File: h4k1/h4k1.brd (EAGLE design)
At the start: 1438.9 x 393.4 mm, 159 parts, among them IC1 STM32F10XCXT6, K1 CHERRY-MX-LED, K10 CHERRY-MX-LED, K11 CHERRY-MX-LED, K12 CHERRY-MX-LED, K13 CHERRY-MX-LED, K14 CHERRY-MX-LED, K15 CHERRY-MX-LED, K16 CHERRY-MX-LED, K17 CHERRY-MX-LED, K18 CHERRY-MX-LED, K19 CHERRY-MX-LED, K2 CHERRY-MX-LED, K20 CHERRY-MX-LED, K21 CHERRY-MX-LED, K22 CHERRY-MX-LED, K23 CHERRY-MX-LED, K24 CHERRY-MX-LED, K25 CHERRY-MX-LED, K26 CHERRY-MX-LED, K27 CHERRY-MX-LED, K28 CHERRY-MX-LED, K29 CHERRY-MX-LED, K3 CHERRY-MX-LED, K30 CHERRY-MX-LED, K31 CHERRY-MX-LED, K32 CHERRY-MX-LED, K33 CHERRY-MX-LED, K34 CHERRY-MX-LED, K35 CHERRY-MX-LED, K36 CHERRY-MX-LED, K37 CHERRY-MX-LED, K38 CHERRY-MX-LED, K39 CHERRY-MX-LED, K4 CHERRY-MX-LED, K40 CHERRY-MX-LED, K41 CHERRY-MX-LED, K42 CHERRY-MX-LED, K43 CHERRY-MX-LED, K44 CHERRY-MX-LED, K45 CHERRY-MX-LED, K46 CHERRY-MX-LED, K47 CHERRY-MX-LED, K48 CHERRY-MX-LED, K49 CHERRY-MX-LED, K5 CHERRY-MX-LED, K50 CHERRY-MX-LED, K51 CHERRY-MX-LED, K52 CHERRY-MX-LED, K53 CHERRY-MX-LED, K54 CHERRY-MX-LED, K55 CHERRY-MX-LED, K56 CHERRY-MX-LED, K57 CHERRY-MX-LED, K58 CHERRY-MX-LED, K59 CHERRY-MX-LED, K6 CHERRY-MX-LED, K60 CHERRY-MX-LED, K61 CHERRY-MX-LED, K62 CHERRY-MX-LED, K63 CHERRY-MX-LED, K64 CHERRY-MX-LED, K7 CHERRY-MX-LED, K8 CHERRY-MX-LED, K9 CHERRY-MX-LED

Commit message: add usb hub
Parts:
- added C10, C11: 4.7uF, hqc-basic:0603
- added C12, C13, C14, C15, C16, C18: 100nF, hqc-basic:0603
- added C17, C19: 10uF, hqc-basic:0603
- added L2: 10uH, hqc-basic:0603
- added R19: 0, hqc-basic:0603
- added R20: 680, hqc-basic:0603
- added R21, R22, R23, R24, R25: 10k, hqc-basic:0603
- added U1: G850G, hqc-communication:SSOP28
- added U2: (no value), hqc-power:SOT223
- added X3: (no value), hqc-crystal:49S
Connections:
- new net 3V3: C18.P$2, C19.P$2, L2.P$1, R22.P$2, U1.16, U1.24, U2.2
- new net 5V: C16.P$2, C17.P$2, R19.P$2, R21.P$1, R25.P$2, U1.23, U2.3
- new net AVDD: C12.P$2, C13.P$2, C14.P$2, L2.P$2, U1.1, U1.10, U1.5
- new net HOST_USB+: U1.26
- new net HOST_USB-: U1.25
- new net N$24: C15.P$2, R21.P$2, U1.13
- new net N$26: R20.P$2, U1.4
- new net N$28: R22.P$1, U1.18
- new net N$30: R23.P$1, U1.17
- new net N$34: R24.P$1, R25.P$1, U1.21
- new net USB1+: U1.28
- new net USB1-: U1.27
- new net USB2+: U1.3
- new net USB2-: U1.2
- new net USB3+: U1.9
- new net USB3-: U1.8
- new net USB4+: U1.12
- new net USB4-: U1.11
- new net VBUS: R19.P$1
- new net X1: C10.P$2, U1.6, X3.P$1
- new net X2: C11.P$2, U1.7, X3.P$2
- net GND: now also C10.P$1, C11.P$1, C12.P$1, C13.P$1, C14.P$1, C15.P$1, C16.P$1, C17.P$1, C18.P$1, C19.P$1, R20.P$1, R23.P$2, R24.P$2, U1.14, U1.15, U2.1

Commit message: audio done
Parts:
- added C20, C21: (no value), hqc:0805
- added C22, C23, C24, C25, C26: 1uF, hqc:0805
- added C27: 10uF, hqc:3216-CPOL
- added C28, C29: 22nF, hqc:0805
- added C30, C31: 100uF, hqc:7343-CPOL
- added C32, C33: 1uF, hqc:3216-CPOL
- added J1: (no value), hqc-connector:PH-5AWD
- added J2: PJ-313D-AUDIO-JACK, hqc:PJ-313D
- added R26: 1M, hqc:0805
- added R27, R28: 1.5k, hqc:0805
- added R29, R30: 22, hqc:0805
- added R31, R32: 16, hqc:0805
- added R33, R34: 330, hqc:0805
- added U3: PCM2704CDB, hqc:SSOP28
- added X4: 12M, hqc-crystal:49S
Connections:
- new net AUDIO_L: C32.P$1, J2.P3, J2.P3@2
- new net AUDIO_R: C33.P$1, J2.P2, J2.P2@2
- new net N$32: C20.P$2, R26.P$1, U3.1, X4.P$1
- new net N$36: C21.P$1, R26.P$2, U3.28, X4.P$2
- new net N$38: R29.P$2, U3.8
- new net N$40: R30.P$2, U3.9
- new net N$42: C22.P$1, R27.P$1, R28.P$2, U3.21, U3.25, U3.26, U3.4, U3.7
- new net N$44: C25.P$1, U3.20
- new net N$46: C30.P$2, C32.P$2, R33.P$2
- new net N$48: C24.P$1, U3.13
- new net N$50: R27.P$2, U3.3
- new net N$54: C26.P$1, U3.16
- new net N$55: C27.P$1, U3.18
- new net N$62: C31.P$2, C33.P$2, R34.P$2
- new net N$64: C29.P$1, R32.P$2
- new net N$66: C28.P$1, R31.P$2
- new net SHIELD: J1.P$5
- new net VOUT_L: C28.P$2, C30.P$1, U3.14
- new net VOUT_R: C29.P$2, C31.P$1, U3.15
- net GND: now also C20.P$1, C21.P$2, C22.P$2, C23.P$1, C24.P$2, C25.P$2, C26.P$2, C27.P$2, J1.P$4, J2.P1, J2.P1@2, R31.P$1, R32.P$1, R33.P$1, R34.P$1, U3.11, U3.12, U3.17, U3.19, U3.6
- net HOST_USB+: now also J1.P$3
- net HOST_USB-: now also J1.P$2
- net USB1+: now also R28.P$1, R30.P$1
- net USB1-: now also R29.P$1
- net VBUS: now also C23.P$2, J1.P$1, U3.10
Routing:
- net GND: track 0.00 -> 115.7 mm, vias 0 -> 6
- net N$42: track 0.00 -> 36.3 mm
- net VBUS: track 0.00 -> 27.1 mm, vias 0 -> 2
- net N$36: track 0.00 -> 17.3 mm
- net N$62: track 0.00 -> 16.2 mm
- net N$32: track 0.00 -> 16.1 mm
- net N$46: track 0.00 -> 14.8 mm
- net VOUT_L: track 0.00 -> 12.6 mm
- net VOUT_R: track 0.00 -> 12.5 mm
- net N$40: track 0.00 -> 7.47 mm
- net N$48: track 0.00 -> 7.18 mm
- net N$38: track 0.00 -> 6.95 mm
- net N$50: track 0.00 -> 4.98 mm
- net N$54: track 0.00 -> 4.80 mm
- net USB1+: track 0.00 -> 4.60 mm
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- added copper zone on layer 1, net GND
- added copper zone on layer 16, net GND

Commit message: add usb connector
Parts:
- added J3: USB-AF10, hqc:USB-AF10
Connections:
- net GND: now also J3.P$G
- net USB1+: now also J3.P$D+; no longer R28.P$1, R30.P$1
- net USB1-: now also J3.P$D-; no longer R29.P$1
- net USB2+: now also R28.P$1, R30.P$1
- net USB2-: now also R29.P$1
- net VBUS: now also J3.P$V
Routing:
- net USB1+: track 4.60 -> 0.00 mm
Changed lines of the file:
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@@
 <element name="C33" library="hqc" package="3216-CPOL" value="1uF" x="197.8025" y="285.75" rot="R180"/>
 <element name="J2" library="hqc" package="PJ-313D" value="PJ-313D-AUDIO-JACK" x="223.8375" y="281.6225" rot="R180"/>
+<element name="J3" library="hqc" package="USB-AF10" value="USB-AF10" x="-145.415" y="-289.2425"/>
 </elements>
 <signals>
@@
 <contactref element="J2" pad="P1"/>
 <contactref element="J2" pad="P1@2"/>
+<contactref element="J3" pad="P$G"/>
 <wire x1="-144.2593" y1="-105.41" x2="-144.2593" y2="-110.49" width="0" layer="19" extent="1-1"/>
 <wire x1="-144.2593" y1="-100.33" x2="-144.2593" y2="-105.41" width="0" layer="19" extent="1-1"/>
@@
 <wire x1="-151.6507" y1="-254" x2="-151.6507" y2="-248.92" width="0" layer="19" extent="1-1"/>
 <wire x1="-149.86" y1="-272.51" x2="-151.6507" y2="-254" width="0" layer="19" extent="1-1"/>
+<wire x1="-141.915" y1="-277.8725" x2="-149.86" y2="-272.51" width="0" layer="19" extent="1-1"/>
 <wire x1="172.4025" y1="265.7475" x2="-135.2" y2="-76.49" width="0" layer="19" extent="1-1"/>
 <wire x1="176.825" y1="275.775" x2="180.0225" y2="275.7225" width="0" layer="19" extent="1-1"/>
-<wire x1="223.8375" y1="278.4225" x2="191.135" y2="286.0675" width="0" layer="19" extent="1-16"/>
+<wire x1="223.8375" y1="278.4225" x2="191.135" y2="279.0825" width="0" layer="19" extent="1-1"/>
 <wire x1="223.8375" y1="284.8225" x2="223.8375" y2="278.4225" width="0" layer="19" extent="1-1"/>
 </signal>
@@
 <wire x1="187.325" y1="272.7325" x2="187.325" y2="265.43" width="0.3048" layer="16"/>
 <wire x1="187.325" y1="270.8275" x2="187.325" y2="272.7325" width="0.3048" layer="1"/>
+<contactref element="J3" pad="P$V"/>
 <wire x1="-153.1493" y1="-173.99" x2="187.325" y2="265.43" width="0" layer="19" extent="1-16"/>
 <wire x1="-149.86" y1="-266.51" x2="-153.1493" y2="-173.99" width="0" layer="19" extent="1-1"/>
+<wire x1="-148.915" y1="-277.8725" x2="-149.86" y2="-266.51" width="0" layer="19" extent="1-1"/>
 </signal>
 <signal name="5V">
@@
 <signal name="USB2-">
 <contactref element="U1" pad="2"/>
+<contactref element="R29" pad="P$1"/>
+<wire x1="-149.625" y1="-153.485" x2="181.61" y2="268.9225" width="0" layer="19" extent="1-1"/>
 </signal>
 <signal name="USB2+">
 <contactref element="U1" pad="3"/>
+<contactref element="R30" pad="P$1"/>
+<contactref element="R28" pad="P$1"/>
+<wire x1="179.705" y1="268.9225" x2="183.515" y2="268.9225" width="0" layer="19" extent="1-1"/>
+<wire x1="-148.975" y1="-153.485" x2="179.705" y2="268.9225" width="0" layer="19" extent="1-1"/>
 </signal>
 <signal name="AVDD">
@@
 <signal name="USB1+">
 <contactref element="U1" pad="28"/>
-<contactref element="R30" pad="P$1"/>
-<contactref element="R28" pad="P$1"/>
-<wire x1="179.705" y1="268.9225" x2="180.6575" y2="269.875" width="0.3048" layer="1"/>
-<wire x1="180.6575" y1="269.875" x2="182.5625" y2="269.875" width="0.3048" layer="1"/>
-<wire x1="182.5625" y1="269.875" x2="183.515" y2="268.9225" width="0.3048" layer="1"/>
-<wire x1="-150.275" y1="-146.235" x2="179.705" y2="268.9225" width="0" layer="19" extent="1-1"/>
+<contactref element="J3" pad="P$D+"/>
+<wire x1="-150.275" y1="-146.235" x2="-144.415" y2="-277.8725" width="0" layer="19" extent="1-1"/>
 </signal>
 <signal name="USB1-">
 <contactref element="U1" pad="27"/>
-<contactref element="R29" pad="P$1"/>
-<wire x1="-149.625" y1="-146.235" x2="181.61" y2="268.9225" width="0" layer="19" extent="1-1"/>
+<contactref element="J3" pad="P$D-"/>
+<wire x1="-149.625" y1="-146.235" x2="-146.415" y2="-277.8725" width="0" layer="19" extent="1-1"/>
 </signal>
 <signal name="HOST_USB+">

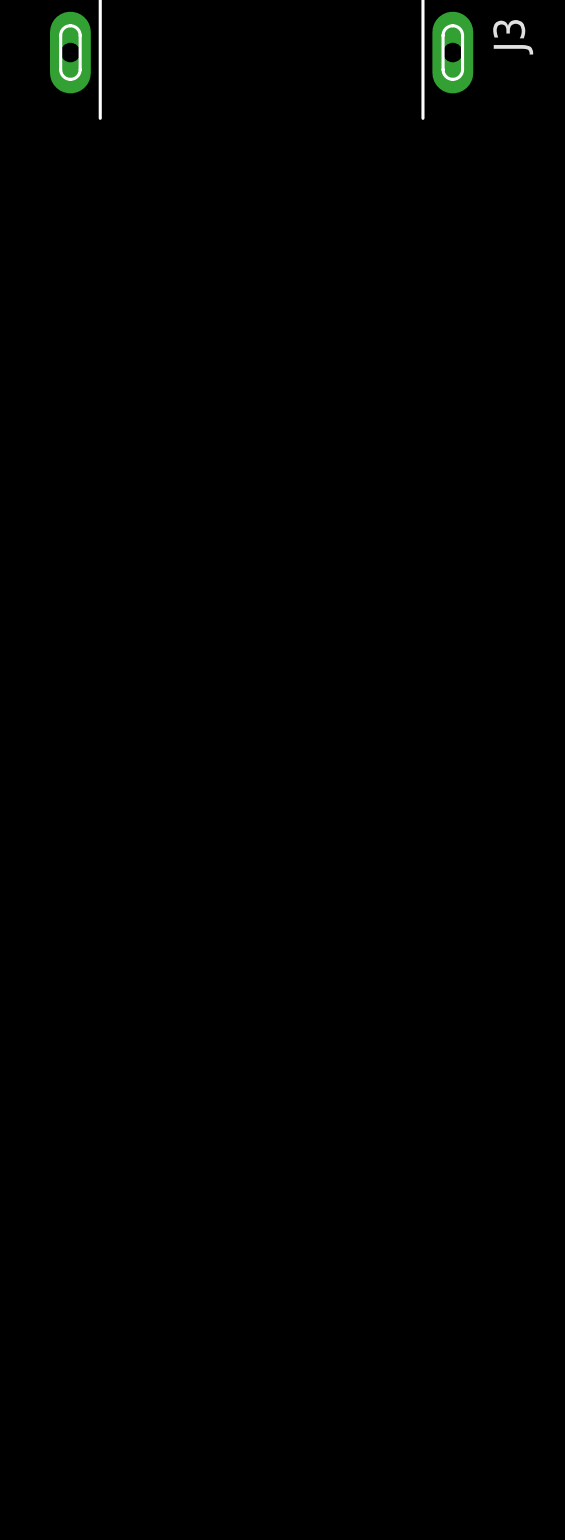
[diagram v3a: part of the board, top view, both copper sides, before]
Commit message: add switches
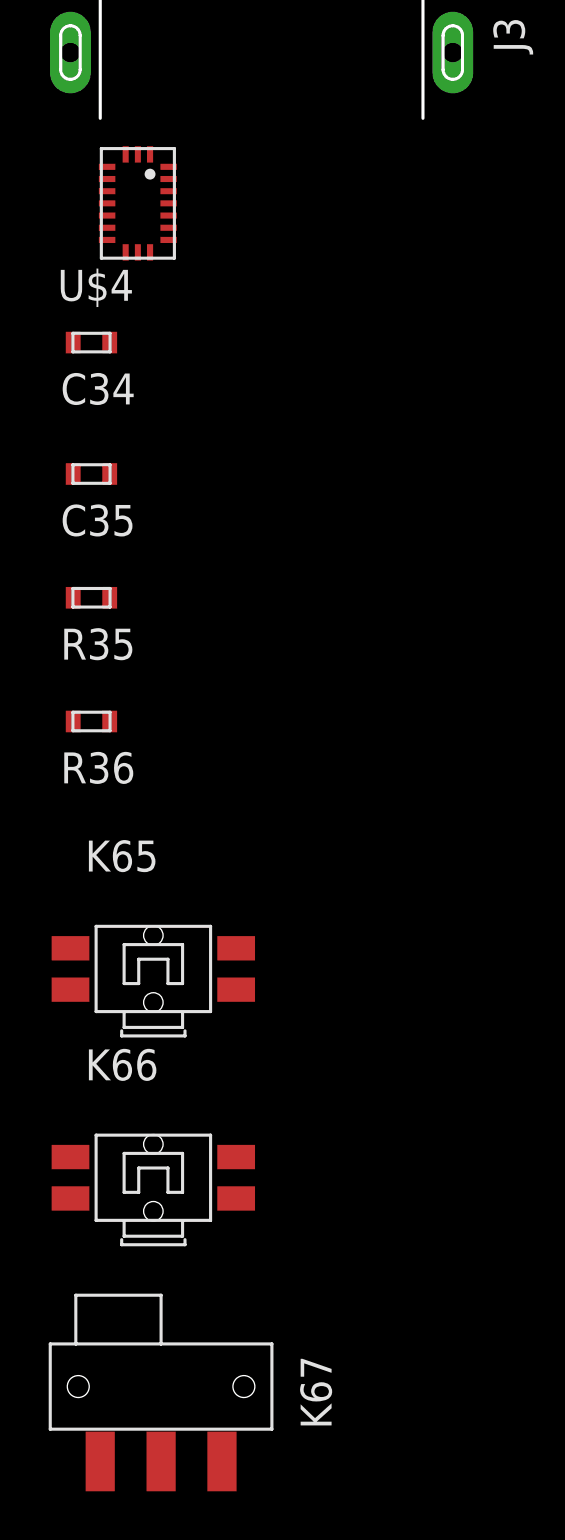
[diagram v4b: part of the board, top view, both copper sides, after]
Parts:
- added C34, C35: 100nF, hqc-basic:0603
- added K65, K66: EVQPUL02K, hqc:EVQPUL
- added K67: K3-1280S-F2, hqc:K3-1280S-F2
- added R35, R36: 4.7k, hqc-basic:0603
- added U$4: BMX055, sensor:BMX055
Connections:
- new net I2C_SCL: IC1.45, R35.P$1, U$4.P$9
- new net I2C_SDA: IC1.46, R36.P$1, U$4.P$11
- net GND: now also C34.P$1, C35.P$1, U$4.P$12, U$4.P$17, U$4.P$20, U$4.P$4, U$4.P$6
- net VDD: now also C34.P$2, C35.P$2, R35.P$2, R36.P$2, U$4.P$13, U$4.P$3, U$4.P$7
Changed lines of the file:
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@@
 <layer number="51" name="tDocu" color="7" fill="1" visible="yes" active="yes"/>
 <layer number="52" name="bDocu" color="7" fill="1" visible="yes" active="yes"/>
+<layer number="53" name="tGND_GNDA" color="7" fill="9" visible="no" active="no"/>
+<layer number="54" name="bGND_GNDA" color="1" fill="9" visible="no" active="no"/>
 <layer number="56" name="wert" color="7" fill="1" visible="no" active="no"/>
 <layer number="90" name="Modules" color="5" fill="1" visible="no" active="no"/>
@@
 <layer number="100" name="Muster" color="7" fill="1" visible="no" active="no"/>
 <layer number="101" name="Patch_Top" color="12" fill="4" visible="yes" active="yes"/>
+<layer number="102" name="Vscore" color="7" fill="1" visible="no" active="yes"/>
+<layer number="104" name="Name" color="7" fill="1" visible="no" active="yes"/>
 <layer number="116" name="Patch_BOT" color="9" fill="4" visible="yes" active="yes"/>
+<layer number="121" name="_tsilk" color="7" fill="1" visible="no" active="yes"/>
+<layer number="122" name="_bsilk" color="7" fill="1" visible="no" active="yes"/>
+<layer number="151" name="HeatSink" color="7" fill="1" visible="no" active="yes"/>
 <layer number="200" name="200bmp" color="1" fill="10" visible="no" active="no"/>
+<layer number="201" name="201bmp" color="2" fill="1" visible="no" active="no"/>
+<layer number="202" name="202bmp" color="3" fill="1" visible="no" active="no"/>
+<layer number="203" name="203bmp" color="4" fill="10" visible="no" active="yes"/>
+<layer number="204" name="204bmp" color="5" fill="10" visible="no" active="yes"/>
+<layer number="205" name="205bmp" color="6" fill="10" visible="no" active="yes"/>
+<layer number="206" name="206bmp" color="7" fill="10" visible="no" active="yes"/>
+<layer number="207" name="207bmp" color="8" fill="10" visible="no" active="yes"/>
+<layer number="208" name="208bmp" color="9" fill="10" visible="no" active="yes"/>
+<layer number="231" name="Eagle3D_PG1" color="14" fill="1" visible="no" active="yes"/>
+<layer number="232" name="Eagle3D_PG2" color="14" fill="2" visible="no" active="yes"/>
+<layer number="233" name="Eagle3D_PG3" color="14" fill="4" visible="no" active="yes"/>
 <layer number="250" name="Descript" color="3" fill="1" visible="no" active="no"/>
 <layer number="251" name="SMDround" color="12" fill="11" visible="no" active="no"/>
@@
 <classes>
 <class number="0" name="default" width="0" drill="0">
+<clearance class="0" value="0.205"/>
 </class>
 </classes>
@@
 <element name="J2" library="hqc" package="PJ-313D" value="PJ-313D-AUDIO-JACK" x="223.8375" y="281.6225" rot="R180"/>
 <element name="J3" library="hqc" package="USB-AF10" value="USB-AF10" x="-145.415" y="-289.2425"/>
+<element name="U$4" library="sensor" package="BMX055" value="BMX055" x="-150.495" y="-292.735"/>
+<element name="C34" library="hqc-basic" package="0603" value="100nF" x="-152.4" y="-298.45"/>
+<element name="C35" library="hqc-basic" package="0603" value="100nF" x="-152.4" y="-303.8475"/>
+<element name="R35" library="hqc-basic" package="0603" value="4.7k" x="-152.4" y="-308.9275"/>
+<element name="R36" library="hqc-basic" package="0603" value="4.7k" x="-152.4" y="-314.0075"/>
+<element name="K65" library="hqc" package="EVQPUL" value="EVQPUL02K" x="-149.86" y="-324.1675"/>
+<element name="K66" library="hqc" package="EVQPUL" value="EVQPUL02K" x="-149.86" y="-332.74"/>
+<element name="K67" library="hqc" package="K3-1280S-F2" value="K3-1280S-F2" x="-149.5425" y="-341.3125"/>
 </elements>
 <signals>
@@
 <contactref element="R18" pad="P$2"/>
 <contactref element="IC1" pad="1"/>
+<contactref element="U$4" pad="P$3"/>
+<contactref element="U$4" pad="P$13"/>
+<contactref element="U$4" pad="P$7"/>
+<contactref element="C34" pad="P$2"/>
+<contactref element="C35" pad="P$2"/>
+<contactref element="R36" pad="P$2"/>
+<contactref element="R35" pad="P$2"/>
 <wire x1="-142.7607" y1="-96.52" x2="-142.7607" y2="-100.33" width="0" layer="19" extent="1-1"/>
 <wire x1="-142.7607" y1="-92.71" x2="-142.7607" y2="-96.52" width="0" layer="19" extent="1-1"/>
@@
 <wire x1="-142.7607" y1="-5.08" x2="-142.7607" y2="-8.89" width="0" layer="19" extent="1-1"/>
 <wire x1="-142.7607" y1="-1.27" x2="-142.7607" y2="-5.08" width="0" layer="19" extent="1-1"/>
+<wire x1="-149.2325" y1="-292.235" x2="-142.7607" y2="-135.89" width="0" layer="19" extent="1-1"/>
+<wire x1="-149.2325" y1="-294.235" x2="-149.2325" y2="-292.235" width="0" layer="19" extent="1-1"/>
+<wire x1="-151.7575" y1="-293.235" x2="-149.2325" y2="-292.235" width="0" layer="19" extent="1-1"/>
+<wire x1="-151.6507" y1="-298.45" x2="-149.2325" y2="-294.235" width="0" layer="19" extent="1-1"/>
+<wire x1="-151.6507" y1="-303.8475" x2="-151.6507" y2="-298.45" width="0" layer="19" extent="1-1"/>
+<wire x1="-151.6507" y1="-308.9275" x2="-151.6507" y2="-303.8475" width="0" layer="19" extent="1-1"/>
+<wire x1="-151.6507" y1="-314.0075" x2="-151.6507" y2="-308.9275" width="0" layer="19" extent="1-1"/>
 </signal>
 <signal name="KB_C1">
@@
 <contactref element="J2" pad="P1@2"/>
 <contactref element="J3" pad="P$G"/>
+<contactref element="U$4" pad="P$4"/>
+<contactref element="U$4" pad="P$6"/>
+<contactref element="C34" pad="P$1"/>
+<contactref element="C35" pad="P$1"/>
+<contactref element="U$4" pad="P$17"/>
+<contactref element="U$4" pad="P$20"/>
+<contactref element="U$4" pad="P$12"/>
 <wire x1="-144.2593" y1="-105.41" x2="-144.2593" y2="-110.49" width="0" layer="19" extent="1-1"/>
 <wire x1="-144.2593" y1="-100.33" x2="-144.2593" y2="-105.41" width="0" layer="19" extent="1-1"/>
@@
 <wire x1="-149.86" y1="-272.51" x2="-151.6507" y2="-254" width="0" layer="19" extent="1-1"/>
 <wire x1="-141.915" y1="-277.8725" x2="-149.86" y2="-272.51" width="0" layer="19" extent="1-1"/>
+<wire x1="-149.995" y1="-290.7225" x2="-141.915" y2="-277.8725" width="0" layer="19" extent="1-1"/>
+<wire x1="-151.7575" y1="-291.235" x2="-149.995" y2="-290.7225" width="0" layer="19" extent="1-1"/>
+<wire x1="-149.2325" y1="-292.735" x2="-149.995" y2="-290.7225" width="0" layer="19" extent="1-1"/>
+<wire x1="-149.2325" y1="-293.735" x2="-149.2325" y2="-292.735" width="0" layer="19" extent="1-1"/>
+<wire x1="-151.7575" y1="-293.735" x2="-151.7575" y2="-291.235" width="0" layer="19" extent="1-1"/>
+<wire x1="-153.1493" y1="-298.45" x2="-151.7575" y2="-293.735" width="0" layer="19" extent="1-1"/>
+<wire x1="-153.1493" y1="-303.8475" x2="-153.1493" y2="-298.45" width="0" layer="19" extent="1-1"/>
 <wire x1="172.4025" y1="265.7475" x2="-135.2" y2="-76.49" width="0" layer="19" extent="1-1"/>
 <wire x1="176.825" y1="275.775" x2="180.0225" y2="275.7225" width="0" layer="19" extent="1-1"/>
@@
 <wire x1="199.2025" y1="285.75" x2="220.6375" y2="278.4225" width="0" layer="19" extent="1-1"/>
 </signal>
+<signal name="I2C_SCL">
+<contactref element="U$4" pad="P$9"/>
+<contactref element="IC1" pad="45"/>
+<contactref element="R35" pad="P$1"/>
+<wire x1="-150.495" y1="-294.7475" x2="-144.2" y2="-79.99" width="0" layer="19" extent="1-1"/>
+<wire x1="-153.1493" y1="-308.9275" x2="-150.495" y2="-294.7475" width="0" layer="19" extent="1-1"/>
+</signal>
+<signal name="I2C_SDA">
+<contactref element="U$4" pad="P$11"/>
+<contactref element="IC1" pad="46"/>
+<contactref element="R36" pad="P$1"/>
+<wire x1="-151.7575" y1="-294.235" x2="-144.2" y2="-80.49" width="0" layer="19" extent="1-1"/>
+<wire x1="-153.1493" y1="-314.0075" x2="-151.7575" y2="-294.235" width="0" layer="19" extent="1-1"/>
+</signal>
 </signals>

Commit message: WIP: layout keyboard switches
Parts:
- removed D57, D58, D59, D60, D61, D62, D63, D64: (no value), hqc-basic:SOD-323
- removed K47, K48, K49, K50, K51, K52, K53, K54, K55, K56, K57, K58, K59, K60, K61, K62, K63, K64: CHERRY-MX-LED, cherrymx:CHERRY-MX-LED
- K1, K10, K2, K20, K21, K22, K3, K33, K34, K35, K36, K37, K38, K39, K4, K40, K41, K42, K43, K44, K45, K46, K5, K6, K7, K8, K9: device cherrymx:CHERRY-MX-LED -> hqc:CHERRY-MX-LED
- K11, K12, K13, K14, K15, K16, K17, K18, K19, K23, K24, K25, K26, K27, K28, K29, K30, K31, K32: value CHERRY-MX-LED -> CHERRY-MX; device cherrymx:CHERRY-MX-LED -> hqc:CHERRY-MX
- moved D34 360.2 mm to (239.7, 63.1), flipped to the bottom, turned to 180 degrees
- moved K8 351.9 mm to (214.8, 11.0)
- moved D35 347.5 mm to (220.3, 63.1), flipped to the bottom, turned to 180 degrees
- moved D33 347.1 mm to (230.2, 54.1), flipped to the bottom
- moved D10 346.9 mm to (237.2, 24.7), flipped to the bottom, turned to 180 degrees
- moved K32 342.5 mm to (205.2, 49.0)
- moved D9 341.8 mm to (235.0, 16.0), flipped to the bottom
- moved D36 335.5 mm to (201.6, 63.1), flipped to the bottom, turned to 180 degrees
- moved D11 332.7 mm to (215.9, 25.0), flipped to the bottom, turned to 180 degrees
- moved D37 323.3 mm to (182.5, 63.1), flipped to the bottom, turned to 180 degrees
- moved D12 320.8 mm to (196.8, 25.0), flipped to the bottom, turned to 180 degrees
- moved D8 316.0 mm to (213.7, 16.1), flipped to the bottom
- moved D32 316.0 mm to (204.2, 54.1), flipped to the bottom
- moved K7 314.0 mm to (193.4, 11.0)
- moved D38 311.0 mm to (163.5, 63.1), flipped to the bottom, turned to 180 degrees
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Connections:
- removed net KB_R8: K57.SW2, K58.SW2, K59.SW2, K60.SW2, K61.SW2, K62.SW2, K63.SW2, K64.SW2
- removed net N$100: D60.P$2, K60.SW1
- removed net N$101: D61.P$2, K61.SW1
- removed net N$102: D62.P$2, K62.SW1
- removed net N$103: D63.P$2, K63.SW1
- removed net N$104: D64.P$2, K64.SW1
- removed net N$85: D47.P$2, K47.SW1
- removed net N$87: D49.P$2, K49.SW1
- removed net N$89: D51.P$2, K51.SW1
- removed net N$91: D52.P$2, K52.SW1
- removed net N$96: D57.P$2, K57.SW1
- removed net N$97: D58.P$2, K58.SW1
- removed net N$98: D59.P$2, K59.SW1
- new net N$68: D47.P$2, K67.P$1
- new net N$70: D49.P$2, K66.P$1, K66.P$3
- net KB_R6: now also K67.P$2; no longer K47.SW2, K48.SW2
- net KB_R7: now also K65.P$2, K65.P$4, K66.P$2, K66.P$4; no longer K49.SW2, K50.SW2, K51.SW2, K52.SW2, K53.SW2, K54.SW2, K55.SW2, K56.SW2
- net N$11: no longer D60.P$1
- net N$13: no longer D61.P$1
- net N$15: no longer D62.P$1
- net N$17: no longer D63.P$1
- net N$2: no longer D57.P$1
- net N$20: no longer D64.P$1
- net N$23: no longer D59.P$1
- net N$5: no longer D58.P$1
- net N$86: now also K67.P$3; no longer K48.SW1
- net N$88: now also K65.P$1, K65.P$3; no longer K50.SW1
- net N$92: no longer K53.SW1
- net N$93: no longer K54.SW1
- net N$94: no longer K55.SW1
- net N$95: no longer K56.SW1
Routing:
- net N$2: track 0.00 -> 321.3 mm, vias 0 -> 6
- net N$5: track 0.00 -> 288.0 mm, vias 0 -> 7
- net N$23: track 0.00 -> 269.3 mm, vias 0 -> 10
- net N$15: track 0.00 -> 259.7 mm, vias 0 -> 8
- net KB_R1: track 0.00 -> 213.6 mm
- net N$11: track 0.00 -> 199.1 mm, vias 0 -> 7
- net N$20: track 0.00 -> 172.5 mm, vias 0 -> 6
- net N$13: track 0.00 -> 163.3 mm, vias 0 -> 6
- net KB_R4: track 0.00 -> 143.7 mm
- net KB_R2: track 0.00 -> 134.9 mm
- net KB_R5: track 0.00 -> 131.6 mm
- net KB_R6: track 0.00 -> 101.3 mm
- net N$17: track 0.00 -> 91.5 mm, vias 0 -> 4
- net KB_R3: track 0.00 -> 88.9 mm
- net N$12: track 0.00 -> 3.53 mm
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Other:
- board size 1438.9 x 393.4 mm -> 250 x 80 mm
